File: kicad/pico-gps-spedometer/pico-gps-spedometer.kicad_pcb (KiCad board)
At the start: 2 copper layers, 98 x 56.5 mm, 28 parts, among them J1 Akkumulátor be, J3 uBlox NEO GPS (6M/8M), Q1 PN2222A, Q2 PN2222A, U1 RP2040-ZERO, U2 DS18B20, U3 LM7805_TO220, U4 TFT_320x240

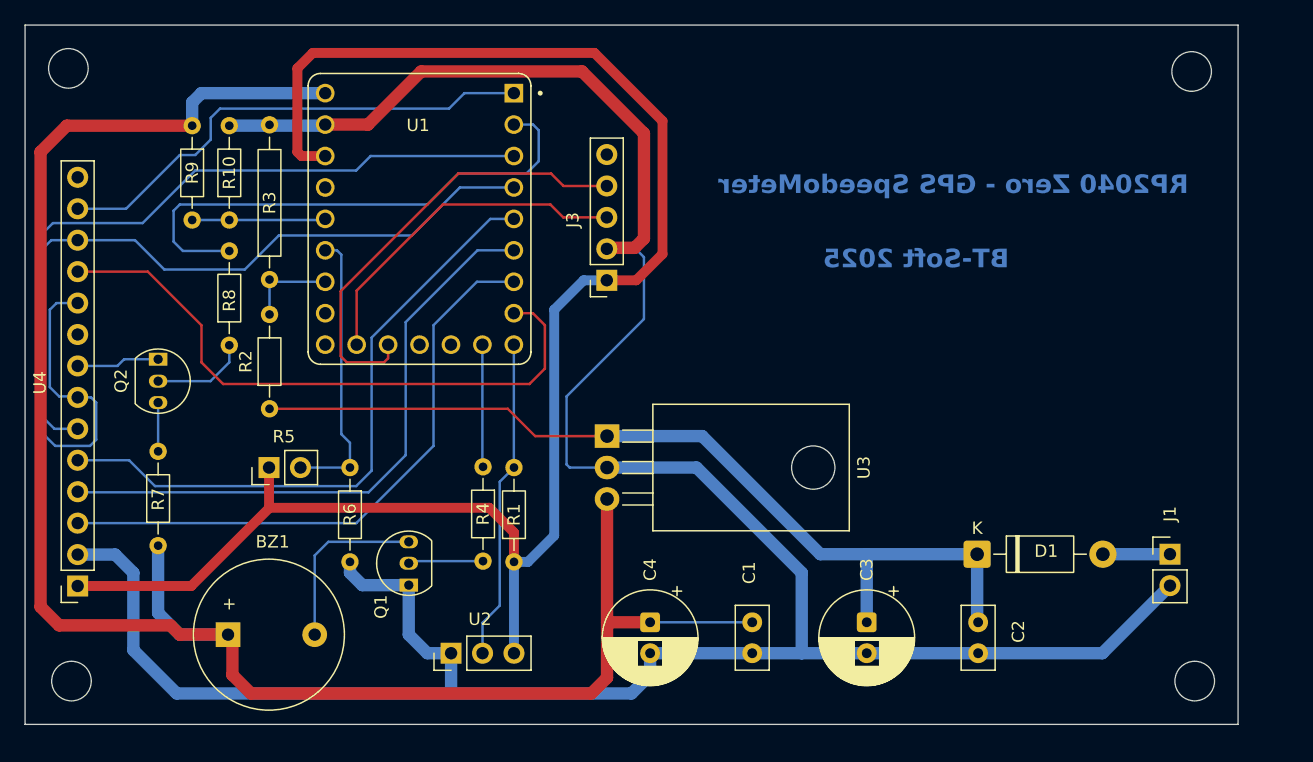
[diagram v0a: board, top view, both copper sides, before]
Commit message: Update visible layers and fix footprint mismatch in pico-gps-spedometer project
- Changed the visible layers setting in the .kicad_prl file to include a new layer.
- Updated the footprint mismatch entry in the .kicad_pro file to correct the dimensions for a specific component.
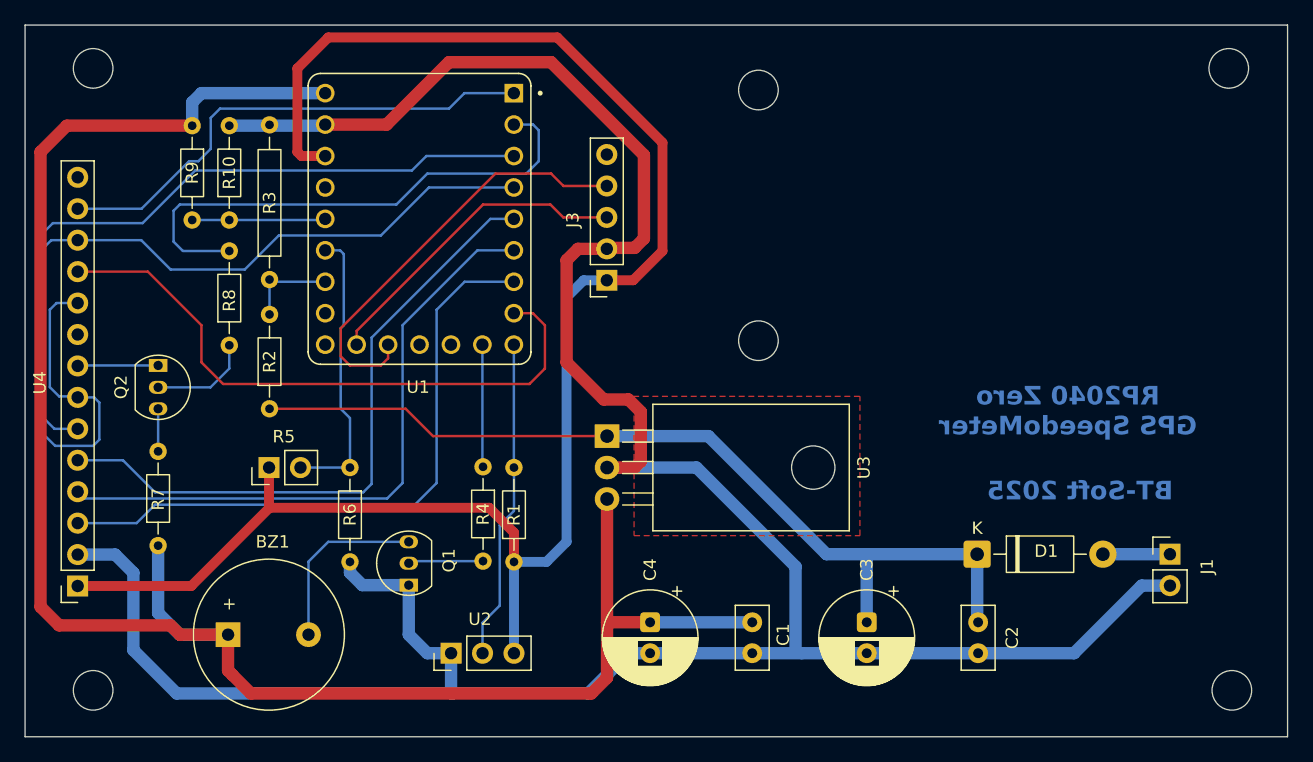
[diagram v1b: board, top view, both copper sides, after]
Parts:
- added REF**: MountingHole_3.2mm_M3, MountingHole:MountingHole_3.2mm_M3, F.Cu at (109.2, 30.2)
- added REF**: MountingHole_3.2mm_M3, MountingHole:MountingHole_3.2mm_M3, F.Cu at (109.2, 50.5)
- moved REF** 3.09 mm to (147.5, 78.8)
- moved REF** 3.01 mm to (147.2, 28.5)
- moved REF** 2.00 mm to (55.5, 28.5)
- moved REF** 1.90 mm to (55.5, 78.8)
- moved Q2 0.50 mm to (60.8, 53.0)
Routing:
- net /CS: track 49.0 -> 51.5 mm
- net GPS_TXD: track 27.9 -> 26.0 mm
- net GND: track 220.0 -> 218.4 mm
- net /RST: track 49.7 -> 51.2 mm
- net GPS_RXD: track 36.4 -> 34.8 mm
- net /DC: track 51.3 -> 52.4 mm
- net +3V3: track 136.9 -> 137.7 mm
- net Net-(Q2-C): track 3.94 -> 3.44 mm
- added copper zone on F.Cu, net GND
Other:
- board size 98 x 56.5 mm -> 102 x 57.5 mm
- board text added: "RP2040 Zero GPS SpeedoMeter"
- board text removed: "RP2040 Zero - GPS SpeedoMeter"
